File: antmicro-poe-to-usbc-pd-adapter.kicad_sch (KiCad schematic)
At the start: 93 parts, among them J1 Bus_RJ45_5-2337992-8, J2 Bus_RJ45_5-2337992-8, J3 USB-C_GCT_USB4105-GF-A, Q1 PJE138K, U1 TPS2372-3RGWR, U2 LV14540DDAR, U3 INA230AIRGTR, U4 IEA48003A280V-001-R, U5 FT4232H_VQFN, U6 TPS65987DDHRSHR, U7 LV14540DDAR, Y1 Resonator_12MHz_ABM8G

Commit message: [#62182] Update resistor fields
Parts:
- C2, R33, R34, R35, R36, R37, R38, R39, R40: DNP DNP -> (none); now in the parts list
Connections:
- net VSS: now also R5.1; no longer R5.2
- net at U1.9 (MPS_DUTY): now also R5.2; no longer R5.1

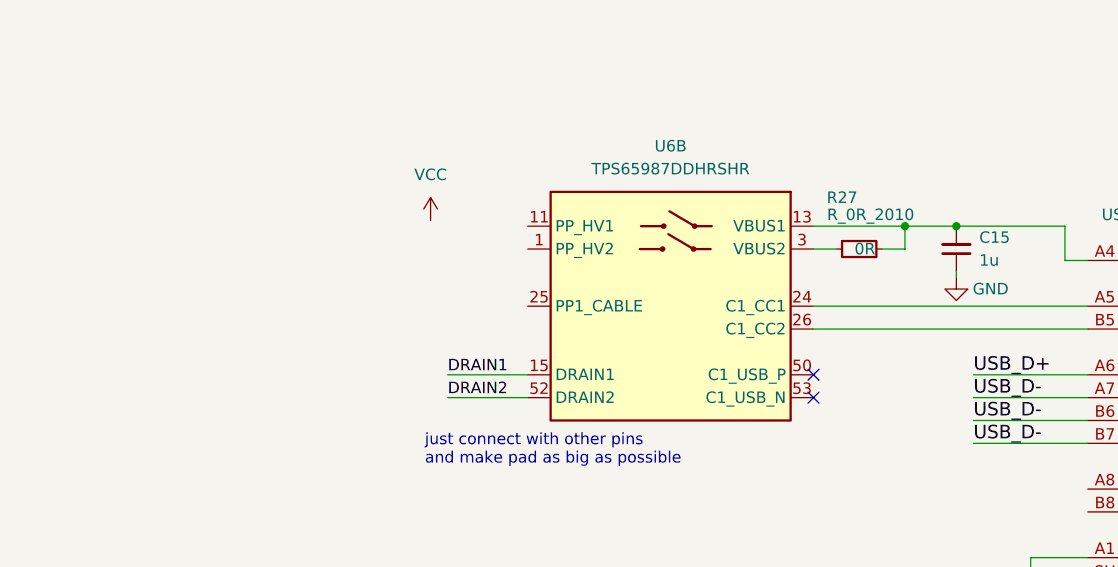
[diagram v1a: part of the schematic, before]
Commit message: [#62182] Tie VBUS1 and VBUS2
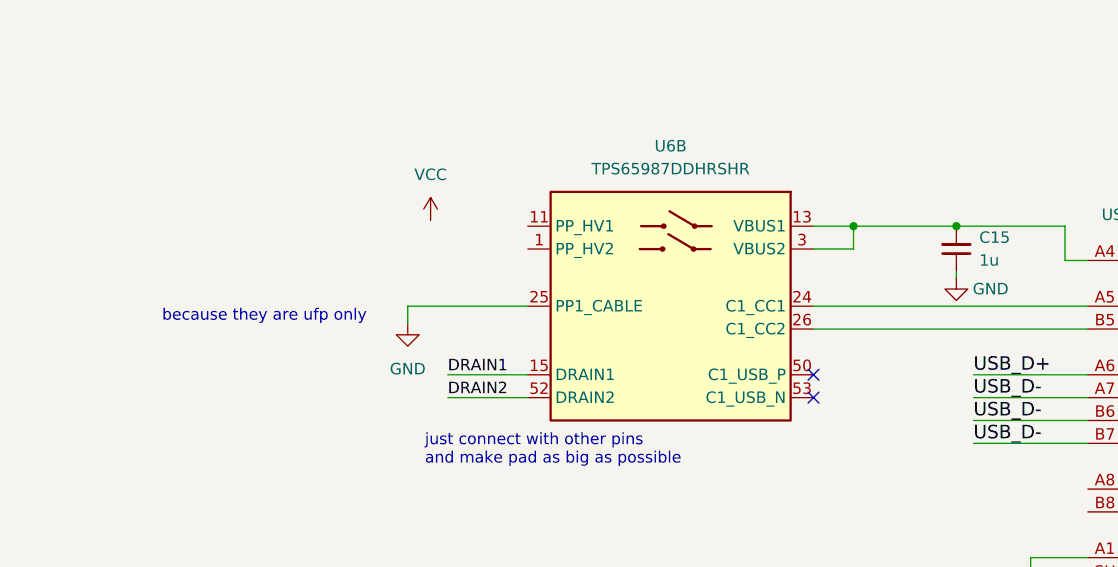
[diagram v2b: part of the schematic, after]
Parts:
- removed R27: R_0R_2010, antmicro-footprints:R_2010_5025Metric, symbol antmicroResistorsmisc:R_0R_2010
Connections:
- net GND: now also U6.25 (PP1_CABLE)
- net at C15.2, J3.A4 (VBUS), J3.A9 (VBUS)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: now also U6.3 (VBUS2)
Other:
- note added: "because they are ufp only"
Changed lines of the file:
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@@
   (junction (at 147.32 132.08) (diameter 0) (color 0 0 0 0)
   )
-  (junction (at 367.03 108.585) (diameter 0) (color 0 0 0 0)
-  )
   (junction (at 313.69 292.735) (diameter 0) (color 0 0 0 0)
   )
@@
   (junction (at 238.76 120.65) (diameter 0) (color 0 0 0 0)
   )
+  (junction (at 361.315 108.585) (diameter 0) (color 0 0 0 0)
+  )
   (junction (at 115.57 334.01) (diameter 0) (color 0 0 0 0)
   )
@@
     (stroke (width 0) (type default))
   )
-  (wire (pts (xy 356.87 108.585) (xy 367.03 108.585))
-    (stroke (width 0) (type default))
-  )
   (wire (pts (xy 132.08 121.92) (xy 151.13 121.92))
     (stroke (width 0) (type default))
@@
     (stroke (width 0) (type default))
   )
+  (wire (pts (xy 325.12 117.475) (xy 311.785 117.475))
+    (stroke (width 0) (type default))
+  )
   (wire (pts (xy 386.08 283.845) (xy 375.92 283.845))
     (stroke (width 0) (type default))
@@
     (stroke (width 0) (type default))
   )
-  (wire (pts (xy 367.03 108.585) (xy 372.745 108.585))
+  (wire (pts (xy 356.87 108.585) (xy 361.315 108.585))
     (stroke (width 0) (type default))
   )
@@
     (stroke (width 0) (type default))
   )
+  (wire (pts (xy 361.315 111.125) (xy 361.315 108.585))
+    (stroke (width 0) (type default))
+  )
   (wire (pts (xy 20.32 328.93) (xy 21.59 328.93))
     (stroke (width 0) (type default))
@@
     (stroke (width 0) (type default))
   )
-  (wire (pts (xy 367.03 108.585) (xy 367.03 111.125))
-    (stroke (width 0) (type default))
-  )
   (bus (pts (xy 49.53 67.31) (xy 49.53 72.39))
     (stroke (width 0) (type default))
@@
     (stroke (width 0) (type default))
   )
+  (wire (pts (xy 311.785 117.475) (xy 311.785 119.38))
+    (stroke (width 0) (type default))
+  )
   (wire (pts (xy 231.14 361.95) (xy 234.95 361.95))
     (stroke (width 0) (type default))
@@
     (stroke (width 0) (type default))
   )
-  (wire (pts (xy 132.08 132.08) (xy 135.89 132.08))
+  (wire (pts (xy 361.315 108.585) (xy 372.745 108.585))
     (stroke (width 0) (type default))
   )
-  (wire (pts (xy 364.49 111.125) (xy 367.03 111.125))
+  (wire (pts (xy 132.08 132.08) (xy 135.89 132.08))
     (stroke (width 0) (type default))
   )
@@
     (stroke (width 0) (type default))
   )
-  (wire (pts (xy 356.87 111.125) (xy 359.41 111.125))
+  (wire (pts (xy 356.87 111.125) (xy 361.315 111.125))
     (stroke (width 0) (type default))
   )
@@
     (effects (font (size 1.27 1.27)) (justify left bottom))
   )
+  (text "because they are ufp only" (at 284.48 119.38 0)
+    (effects (font (size 1.27 1.27)) (justify left bottom))
+  )
   (text "Nlogic same \nas Orin" (at 203.2 111.76 0)
     (effects (font (size 1.27 1.27)) (justify left bottom))
@@
     )
   )
+  (symbol (lib_id "antmicropower:GND") (at 311.785 119.38 0) (unit 1)
+    (in_bom yes) (on_board yes) (dnp no) (fields_autoplaced)
+    (property "Reference" "#PWR070" (at 320.675 121.92 0)
+      (effects (font (size 1.27 1.27) (thickness 0.15)) (justify left bottom) hide)
+    )
+    (property "Value" "GND" (at 311.785 124.46 0)
+      (effects (font (size 1.27 1.27) (thickness 0.15)))
+    )
+    (property "Footprint" "" (at 320.675 127 0)
+      (effects (font (size 1.27 1.27) (thickness 0.15)) (justify left bottom) hide)
+    )
+    (property "Datasheet" "" (at 320.675 132.08 0)
+      (effects (font (size 1.27 1.27) (thickness 0.15)) (justify left bottom) hide)
+    )
+    (property "Author" "Antmicro" (at 320.675 127 0)
+      (effects (font (size 1.27 1.27) (thickness 0.15)) (justify left bottom) hide)
+    )
+    (property "License" "Apache-2.0" (at 320.675 129.54 0)
+      (effects (font (size 1.27 1.27) (thickness 0.15)) (justify left bottom) hide)
+    )
+    (pin "1")
+    (instances
+      (project "antmicro-poe-to-usbc-pd-adapter"
+        (path "/cf0d4429-3f03-449f-96a7-26d69371a46d"
+          (reference "#PWR070") (unit 1)
+        )
+      )
+    )
+  )
   (symbol (lib_id "antmicroResistors0402:R_24k9_0402") (at 135.89 109.22 270) (unit 1)
     (in_bom yes) (on_board yes) (dnp no) (fields_autoplaced)
@@
         )
       )
-    )
-  )
-  (symbol (lib_id "antmicroResistorsmisc:R_0R_2010") (at 359.41 111.125 0) (unit 1)
-    (in_bom yes) (on_board yes) (dnp no)
-    (property "Reference" "R27" (at 360.045 105.41 0)
-      (effects (font (size 1.27 1.27) (thickness 0.15)))
-    )
-    (property "Value" "R_0R_2010" (at 363.22 107.315 0)
-      (effects (font (size 1.27 1.27) (thickness 0.15)))
-    )
-    (property "Footprint" "antmicro-footprints:R_2010_5025Metric" (at 374.65 121.285 0)
-      (effects (font (size 1.27 1.27) (thickness 0.15)) (justify left bottom) hide)
-    )
-    (property "Datasheet" "https://www.vishay.com/docs/20035/dcrcwe3.pdf" (at 374.65 123.825 0)
-      (effects (font (size 1.27 1.27) (thickness 0.15)) (justify left bottom) hide)
-    )
-    (property "MPN" "CRCW20100000Z0EF" (at 374.65 126.365 0)
-      (effects (font (size 1.27 1.27) (thickness 0.15)) (justify left bottom) hide)
-    )
-    (property "Manufacturer" "Vishay" (at 374.65 128.905 0)
-      (effects (font (size 1.27 1.27) (thickness 0.15)) (justify left bottom) hide)
-    )
-    (property "Val" "0R " (at 362.585 111.125 0)
-      (effects (font (size 1.27 1.27) (thickness 0.15)))
-    )
-    (property "Author" "Antmicro" (at 374.65 131.445 0)
-      (effects (font (size 1.27 1.27) (thickness 0.15)) (justify left bottom) hide)
-    )
-    (property "License" "Apache-2.0" (at 374.65 133.985 0)
-      (effects (font (size 1.27 1.27) (thickness 0.15)) (justify left bottom) hide)
-    )
-    (property "Tolerance" "template_tolerance" (at 379.73 121.285 0)
-      (effects (font (size 1.27 1.27)) (justify left bottom) hide)
-    )
-    (pin "1")
-    (pin "2")
-    (instances
-      (project "antmicro-poe-to-usbc-pd-adapter"
-        (path "/cf0d4429-3f03-449f-96a7-26d69371a46d"
-          (reference "R27") (unit 1)
-        )
-      )

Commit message: [#62182] Add mux to flash
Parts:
- added C16, C31: C_4u7_25V_0402, antmicro-footprints:C_0402_1005Metric, symbol antmicroCapacitors0402:C_4u7_25V_0402
- added C32: C_100n_0402, antmicro-footprints:C_0402_1005Metric, symbol antmicroCapacitors0402:C_100n_0402
- added D6: RB521S30T1G, antmicro-footprints:SOD-523, symbol antmicroDiodesRectifiersSingle:RB521S30T1G
- added R27: R_0R_2010, antmicro-footprints:R_2010_5025Metric, symbol antmicroResistorsmisc:R_0R_2010
- added R42, R43: R_1k_0402, antmicro-footprints:R_0402_1005Metric, symbol antmicroResistors0402:R_1k_0402
- added R44: R_0R_0402, antmicro-footprints:R_0402_1005Metric, symbol antmicroResistors0402:R_0R_0402
- added U8: W25Q80DV_SOIC-8, antmicro-footprints:SOIC-8_3.9x4.9x1.75mm_P1.27mm, symbol antmicroMemory:W25Q80DV_SOIC-8
- added U9: 74CBTLV3257_VQFN, antmicro-footprints:DHVQFN-16-1EP_2.5x3.5mm_P0.5mm, symbol antmicroInterfaceAnalogSwitchesMultiplexersDemultiplexers:74CBTLV3257_VQFN
- C15: now not fitted
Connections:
- net +3V3: now also U9.16 (VCC)
- net GND: now also C16.1, C31.1, C32.1, R43.1, U8.4 (VSS), U9.15 (OE), U9.8 (GND); no longer U6.25 (PP1_CABLE)
- net PDC_LDO_3V3: now also D6.2, R42.1, U8.3 (~{WP}/IO2), U8.7 (~{HOLD}/IO3)
- net SCL_FTDI: no longer R19.1, R20.1, U3.5 (SCL), U5.12 (ADBUS0)
- net SDA_FTDI: no longer R22.2, U3.4 (SDA), U5.14 (ADBUS2)
- net VCC: now also U6.1 (PP_HV2), R27.1
- net Vcore: now also C31.2
- net at U6.11 (PP_HV1): now also R27.2
- net FTDI_SCK: now reaches U5.22 (BDBUS0)
- net FTDI_SCK: now also U9.3 (1B2)
- net FTDI_SDO: now reaches U5.23 (BDBUS1)
- net FTDI_SDO: now also U9.6 (2B2)
- net FTDI_SDI: now reaches U5.24 (BDBUS2)
- net FTDI_SDI: now also U9.10 (3B2)
- net FTDI_CS: now reaches U5.25 (BDBUS3)
- net FTDI_CS: now also U9.13 (4B2)
- net FTDI_MUX_SW: now reaches U5.32 (CDBUS0)
- net TPS_SDI: now reaches U6.36 (SPI_POCI)
- net TPS_SDI: now also U9.11 (3B1)
- net TPS_SDO: now reaches U6.37 (SPI_PICO)
- net TPS_SDO: now also U9.5 (2B1)
- net TPS_SCK: now reaches U6.38 (SPI_CLK)
- net TPS_SCK: now also U9.2 (1B1)
- net TPS_CS: now reaches U6.39 (~{SPI_CS})
- net TPS_CS: now also U9.14 (4B1)
- net WP renamed WP1
- new net: R43.2, R44.1, U9.1 (S)
- new net: C32.2, D6.1, U8.8 (VCC)
- new net +5V: C16.2, U6.25 (PP1_CABLE)
- new net FLASH_CS: U8.1 (~{CS}), U9.12 (4A)
- new net FLASH_SCK: U8.6 (SCLK), U9.4 (1A)
- new net FLASH_SDI: U8.5 (SI/IO0), U9.9 (3A)
- new net FLASH_SDO: R42.2, U8.2 (SO/IO1), U9.7 (2A)
- new net MUX_SW: R44.2
- new net SCL1_FTDI: R19.1, U3.5 (SCL), U5.12 (ADBUS0)
- new net SDA1_FTDI: R20.1, R22.2, U3.4 (SDA), U5.14 (ADBUS2)
- no-connect marks 41 -> 38
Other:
- note added: "in case of mistake"
- note removed: "because they are ufp only"
- moved on the sheet: C11, C12, C13, C14, C25, C26, C27, C28, C29, C30, FB4, FB5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

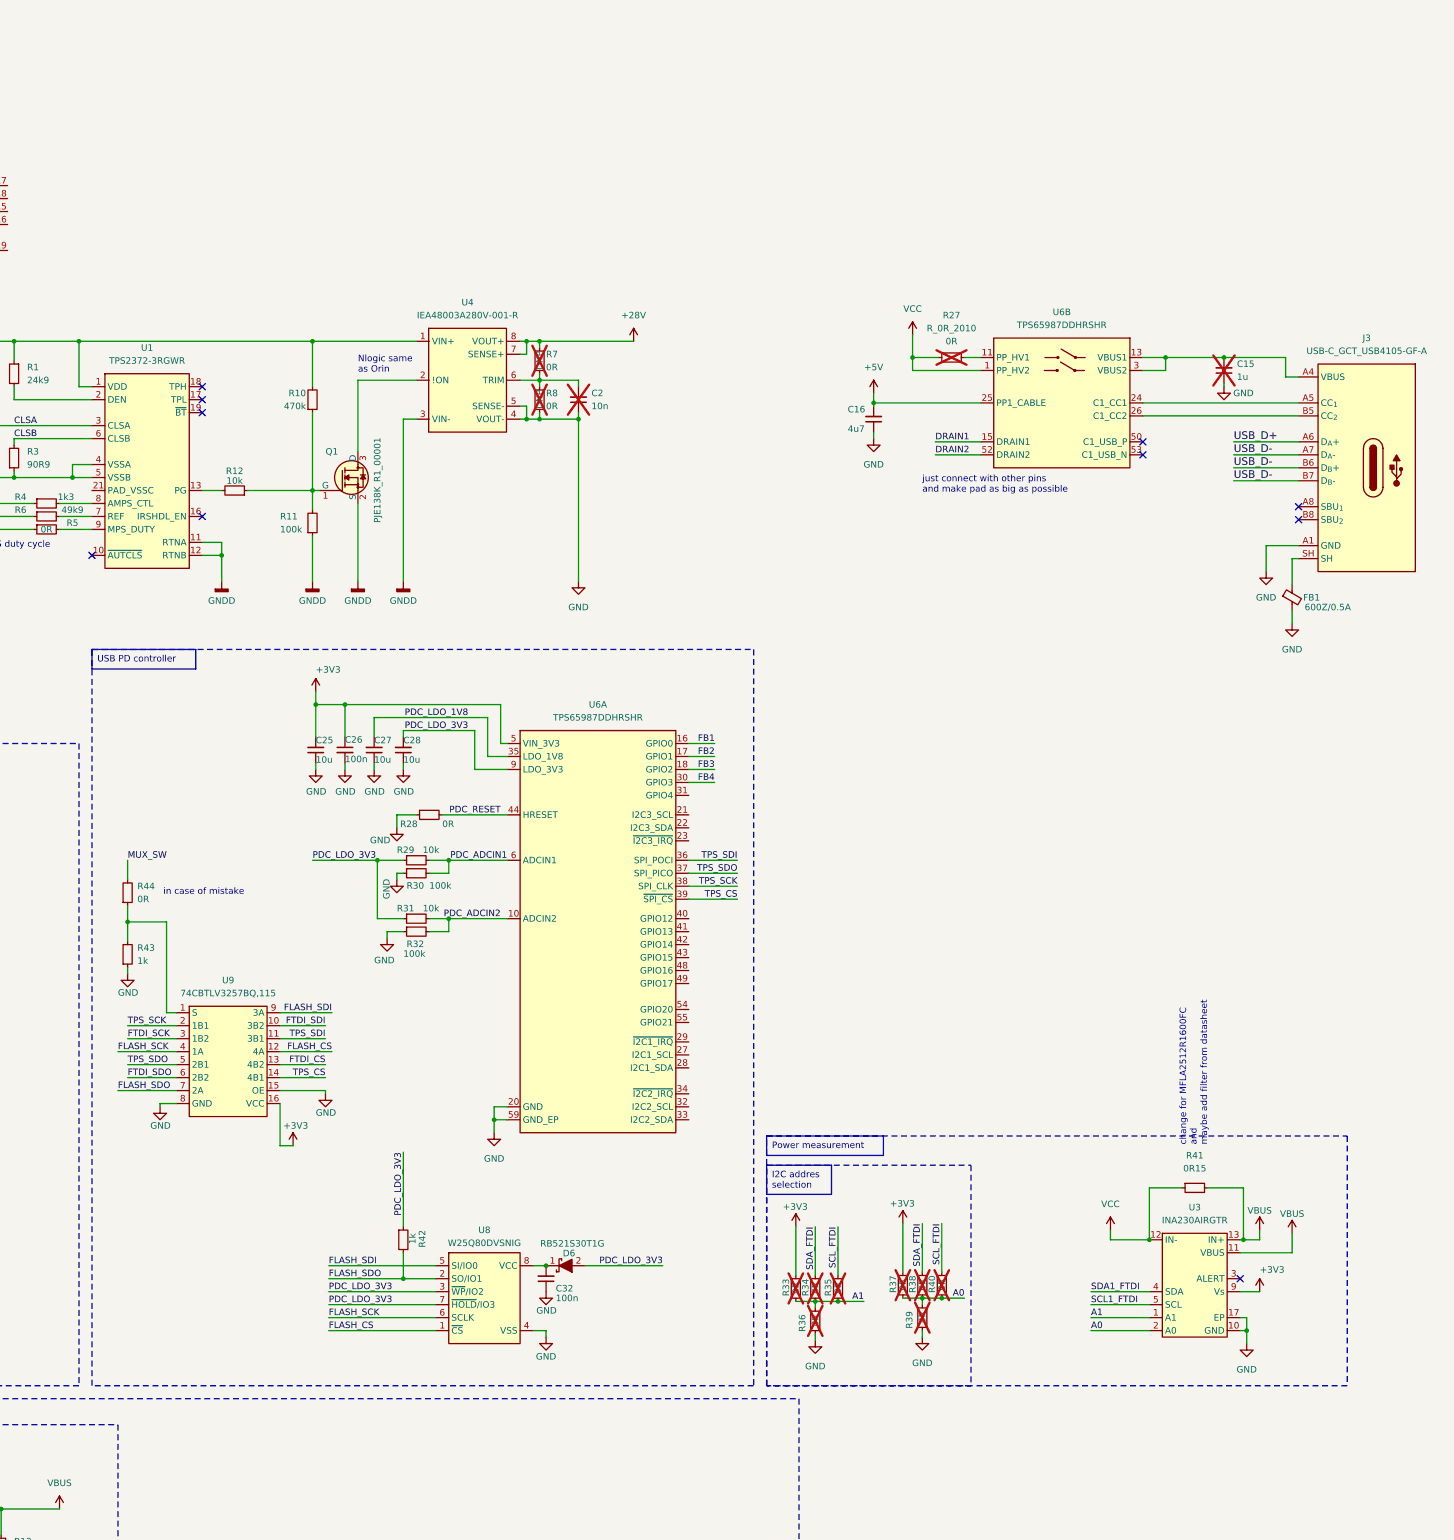
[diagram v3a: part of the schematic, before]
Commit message: [#62182] Clean schematic
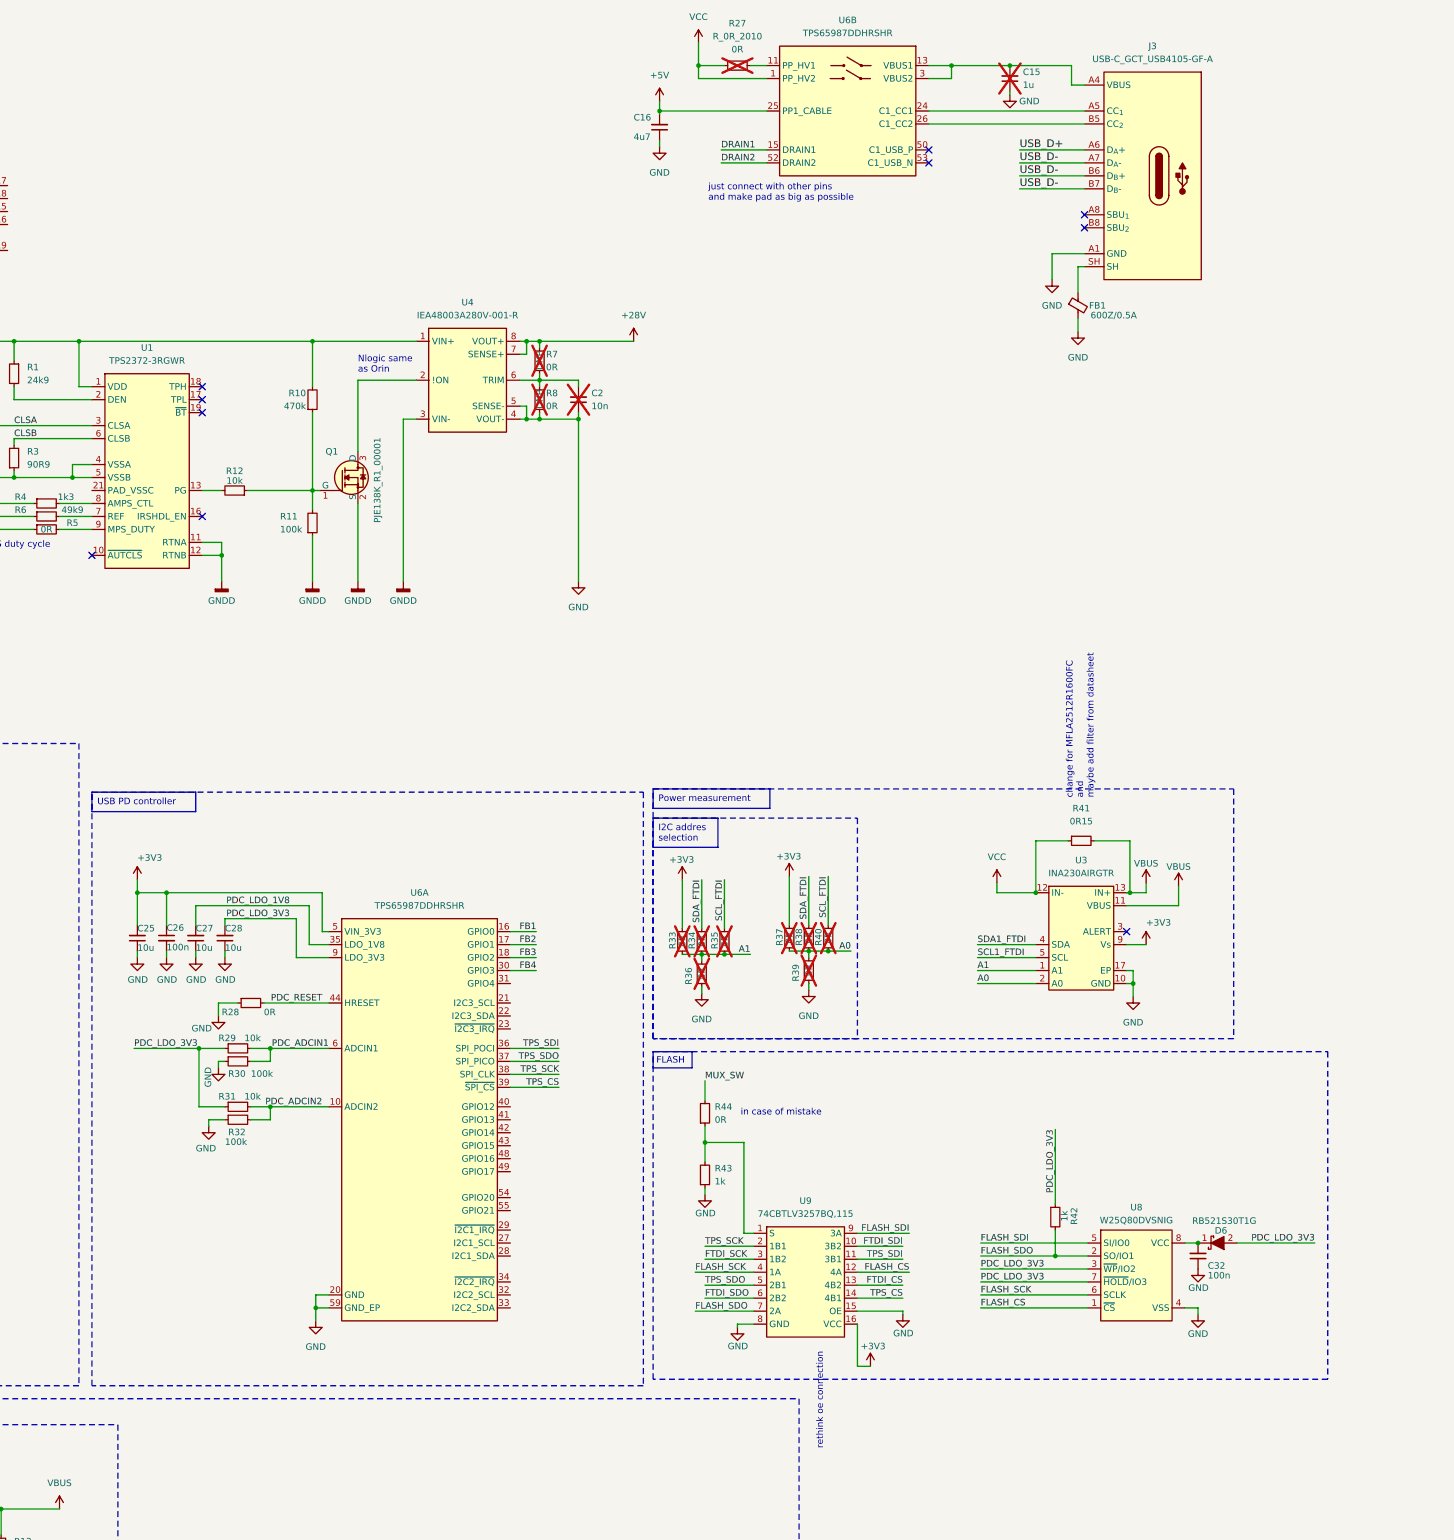
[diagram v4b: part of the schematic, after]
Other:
- note added: "FLASH"
- note added: "rethink oe connection"
- moved on the sheet: C15, C16, C25, C26, C27, C28, C32, D6, FB1, J3, R27, R28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
